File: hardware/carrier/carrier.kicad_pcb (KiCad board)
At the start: 4 copper layers, 165 x 103 mm, 153 parts, among them J1 Harness_4Runner, J2 Pi 4 GPIO, J3 UART, M1 FAN1, M2 FAN2, Q1 BUK7Y4R8-60E, Q2 BUK7Y4R8-60E, Q3 MMBT3904, Q4 MMBT3904, Q5 MMBT3904, Q6 2N7002, Q7 2N7002, U1 LM74800-Q1, U2 ADS1115IDGS, U3 DS3231SN, U4 CAT24C32, U5 LM61460-Q1, U6 TLV75533PDBV, U7 TAS6424E-Q1, U8 CS2100-CP, Y1 12MHz

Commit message: Carrier PCB: Pi geometry from the HAT spec, amplifier block placement
J2 sits on the bottom with pin 1 over the Pi's pin 1 (checked by pad
position), H1-H4 on the Pi hole pattern and isolated per the HAT spec,
USB/Ethernet notch and display-flex cutout follow the Pi's position
(provisional until measured). The TAS6424 block follows TI's EVM layout.
Parts carry a Section field so placement finds them by block and net.
Boot caps move to 0603 to fit the 0.635 mm pitch.

Co-Authored-By: Claude Opus 5.5 <noreply@anthropic.com>
Claude-Session: https://claude.ai/code/session_01EoLoLi7g91W5u4w3UzwQgu
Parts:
- C43, C44, C45, C46, C47, C48, C49, C50: footprint Capacitor_SMD:C_0805_2012Metric -> Capacitor_SMD:C_0603_1608Metric
- H1, H2, H3, H4: footprint MountingHole:MountingHole_2.7mm_M2.5_Pad_Via -> MountingHole:MountingHole_2.7mm_M2.5
- J2: moved to B.Cu
- moved U4 205.7 mm to (118.6, 267.6)
- moved U3 205.7 mm to (106.0, 270.3)
- moved R8 205.1 mm to (113.5, 259.0)
- moved R9 205.1 mm to (119.5, 259.0)
- moved R10 205.1 mm to (125.5, 259.0)
- moved R6 205.1 mm to (101.5, 259.0)
- moved R7 205.1 mm to (107.5, 259.0)
- moved C69 200.6 mm to (322.2, 218.8)
- moved C67 200.6 mm to (310.2, 218.8)
- moved C68 200.6 mm to (316.2, 218.8)
- moved U7 199.8 mm to (208.0, 168.0)
- moved L3 193.9 mm to (240.8, 180.0)
- moved L5 184.2 mm to (240.8, 172.0)
- moved L4 182.9 mm to (226.8, 172.0)
- moved C65 179.5 mm to (246.6, 154.4), turned to 90 degrees
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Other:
- outline, holes or cut-outs redrawn

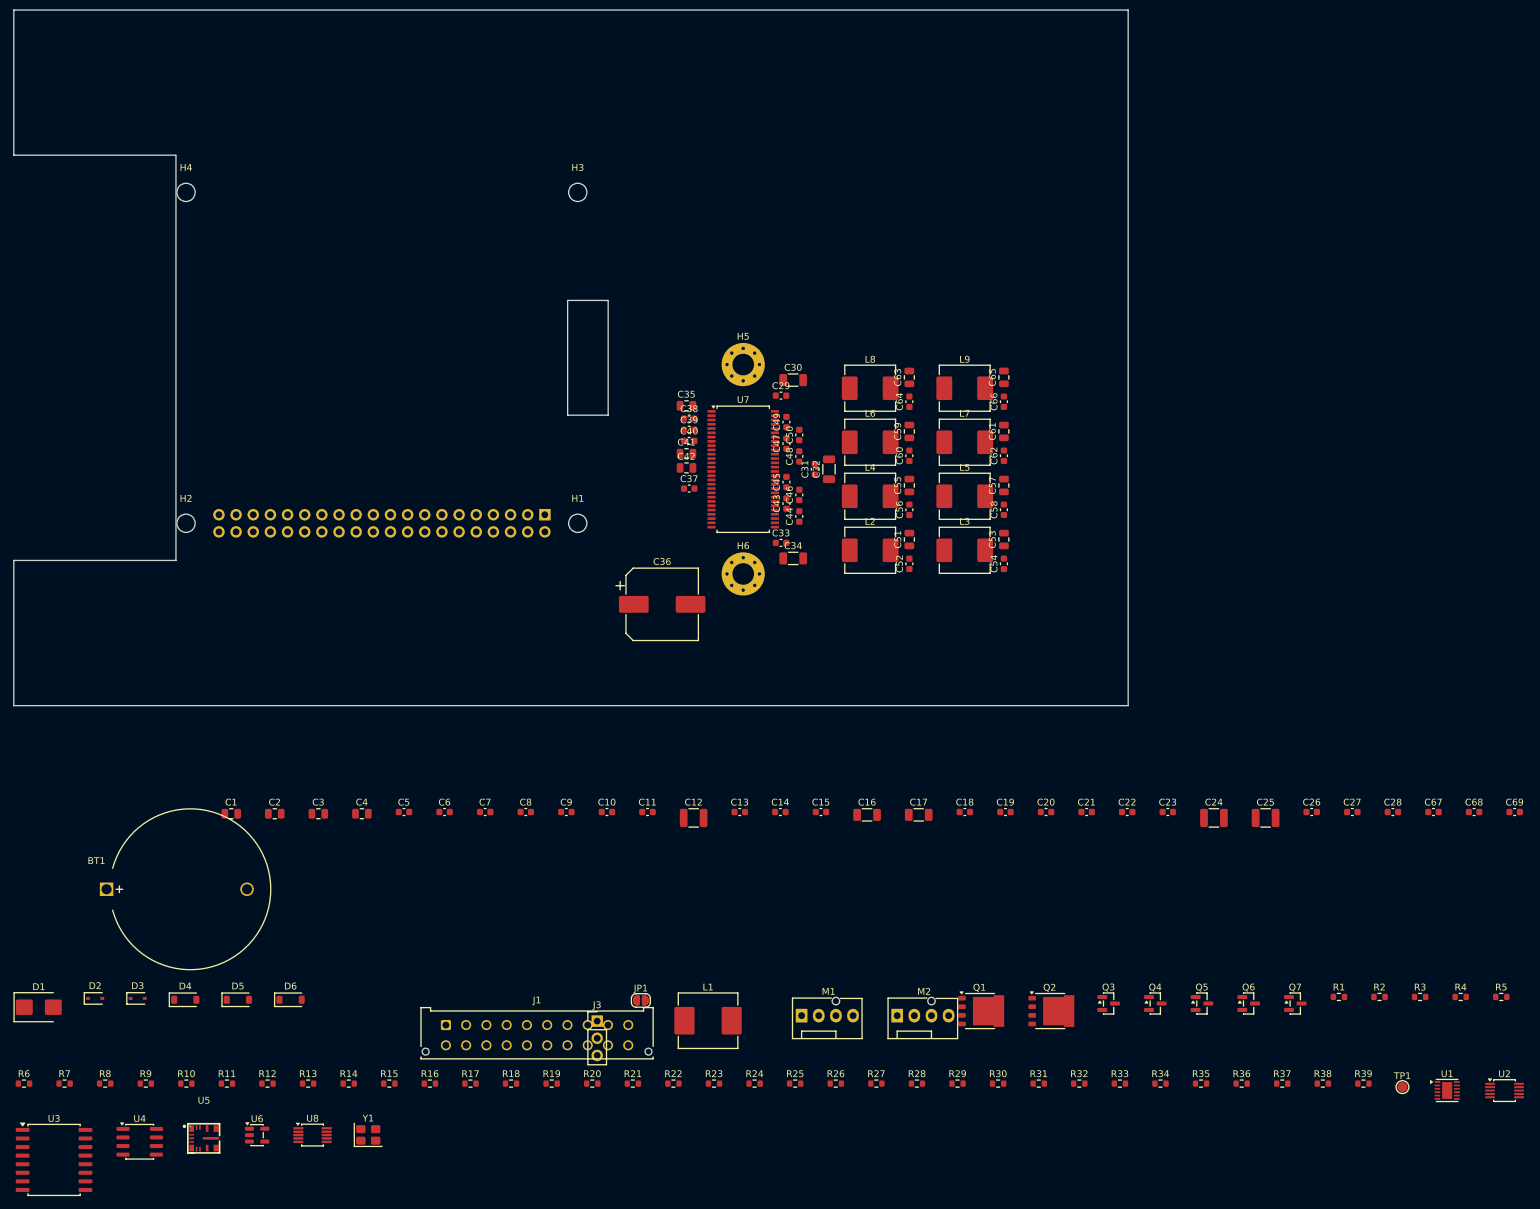
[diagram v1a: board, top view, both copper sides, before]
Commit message: Carrier PCB: place harness, input protection and 5 V buck blocks
Co-Authored-By: Claude Opus 5.5 <noreply@anthropic.com>
Claude-Session: https://claude.ai/code/session_01EoLoLi7g91W5u4w3UzwQgu
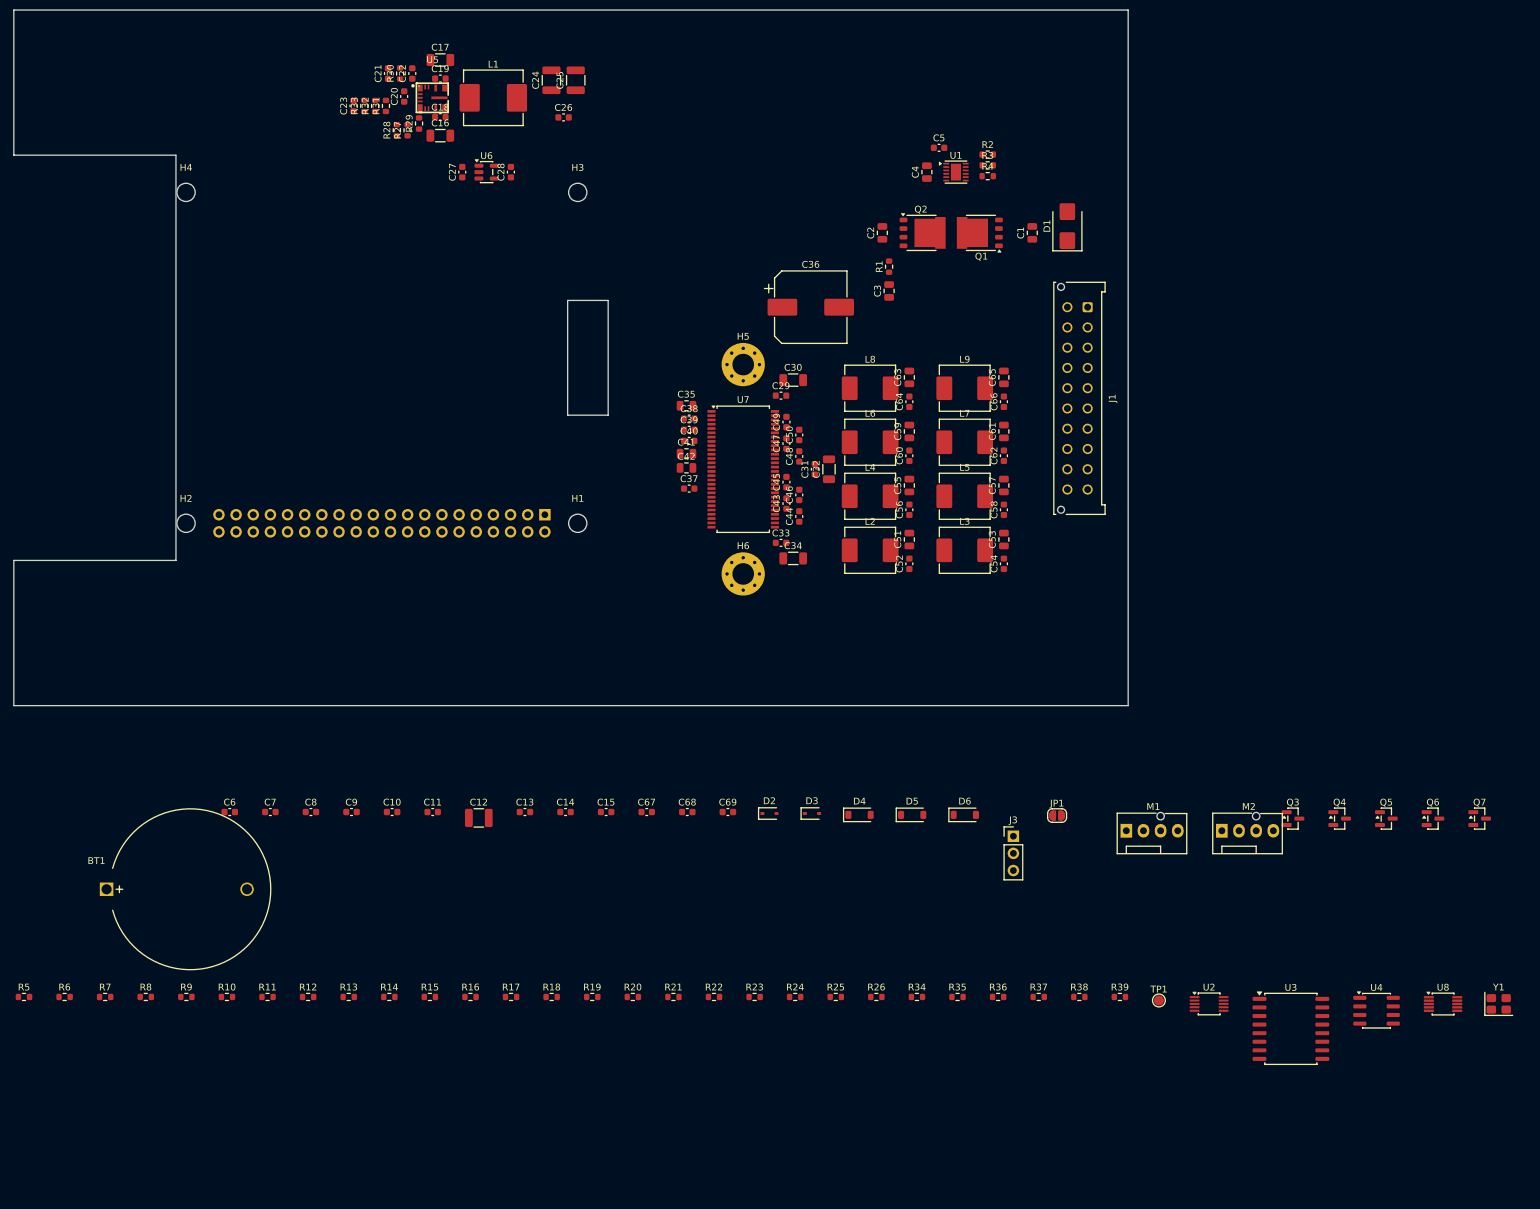
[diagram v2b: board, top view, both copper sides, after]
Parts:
- moved R5 218.7 mm to (101.5, 246.1)
- moved D1 191.2 mm to (256.0, 132.0), turned to 90 degrees
- moved U4 184.2 mm to (301.8, 248.2)
- moved U3 184.2 mm to (289.1, 250.9)
- moved R33 183.0 mm to (151.9, 114.2), turned to 90 degrees
- moved R32 178.4 mm to (153.5, 114.2), turned to 90 degrees
- moved R31 174.1 mm to (155.1, 114.2), turned to 90 degrees
- moved R30 173.8 mm to (157.2, 109.4), turned to 90 degrees
- moved U8 168.5 mm to (311.6, 247.2)
- moved Y1 168.5 mm to (319.9, 247.2)
- moved R29 163.0 mm to (160.0, 116.8), turned to 90 degrees
- moved C27 162.3 mm to (166.4, 124.0), turned to 90 degrees
- moved C28 161.4 mm to (173.6, 124.0), turned to 90 degrees
- moved R28 160.8 mm to (156.7, 117.8), turned to 90 degrees
- moved C23 159.6 mm to (150.3, 114.2), turned to 90 degrees
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
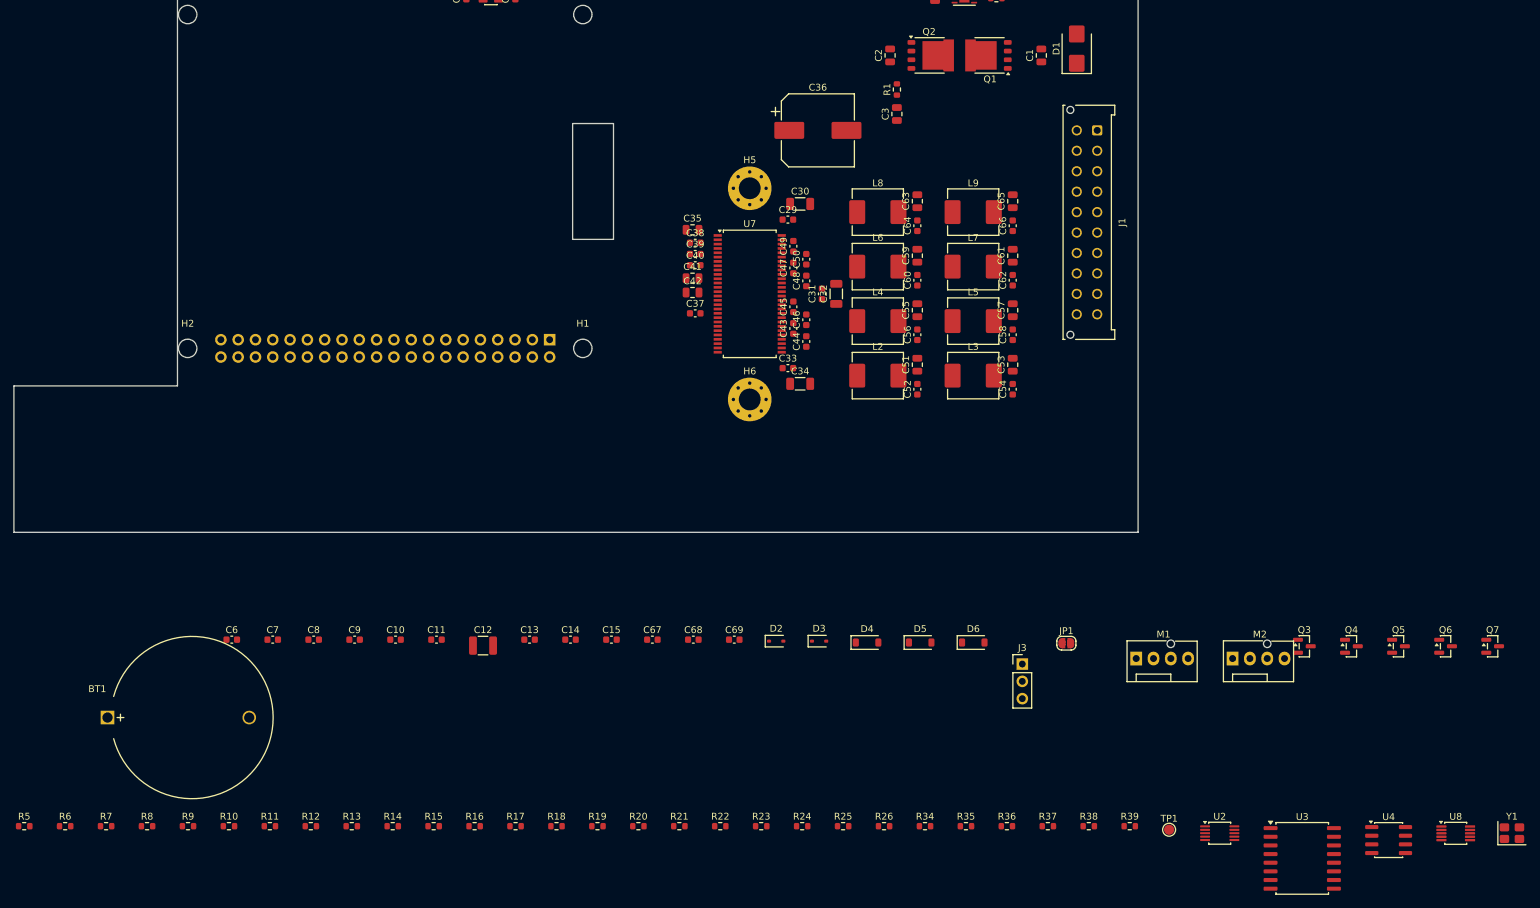
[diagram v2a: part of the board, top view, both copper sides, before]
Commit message: Carrier PCB: place the remaining circuits; every part on the board
RTC, coin cell and ID EEPROM over the Pi, key/lights/reverse sensing and
the wheel ADC beside J1's control pins, fan headers on the bottom edge.
U8 uses the 3x3 TSSOP-10 land pattern (same MO-187 package, wider gaps).
DRC: no overlaps or clearance errors; routing still to do.

Co-Authored-By: Claude Opus 5.5 <noreply@anthropic.com>
Claude-Session: https://claude.ai/code/session_01EoLoLi7g91W5u4w3UzwQgu
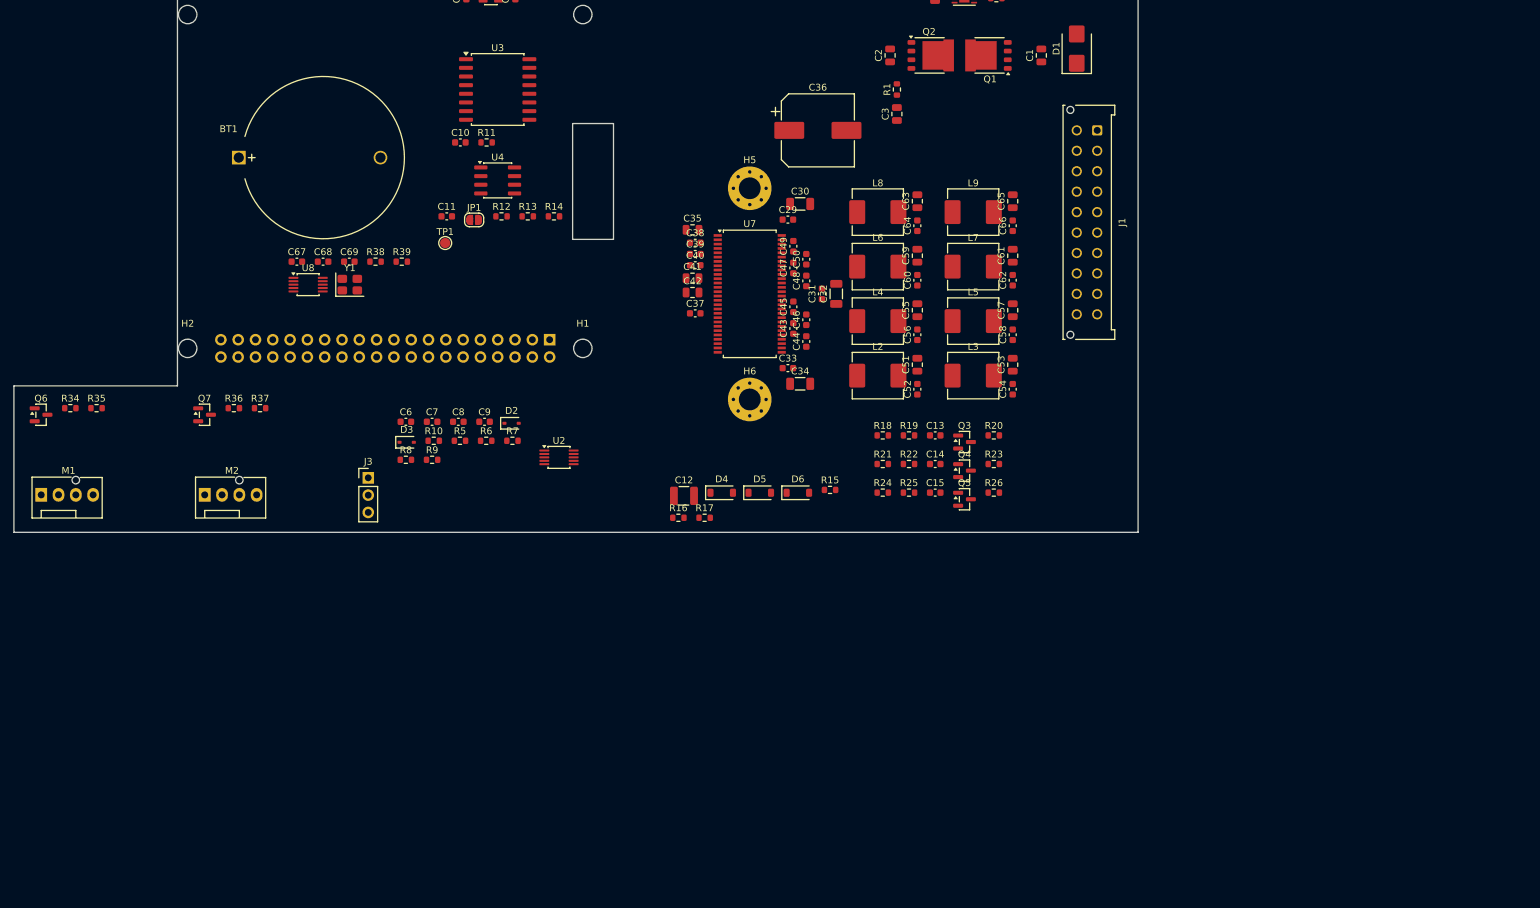
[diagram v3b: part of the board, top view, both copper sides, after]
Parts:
- U8: footprint Package_SO:MSOP-10_3x3mm_P0.5mm -> Package_SO:TSSOP-10_3x3mm_P0.5mm
- moved Q6 208.9 mm to (104.0, 185.7)
- moved Q7 192.1 mm to (128.0, 185.7)
- moved Y1 188.6 mm to (149.3, 166.6)
- moved U8 186.7 mm to (143.2, 166.6)
- moved U3 163.4 mm to (171.0, 138.0)
- moved U4 162.7 mm to (171.0, 151.3)
- moved M1 162.5 mm to (104.0, 197.5)
- moved M2 152.8 mm to (128.0, 197.5)
- moved R35 141.6 mm to (112.1, 184.8)
- moved R34 139.7 mm to (108.3, 184.8)
- moved TP1 136.8 mm to (163.3, 160.5)
- moved R39 135.2 mm to (156.9, 163.3)
- moved R38 133.5 mm to (153.1, 163.3)
- moved R37 130.9 mm to (136.1, 184.8)
- moved R36 129.0 mm to (132.3, 184.8)
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
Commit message: Carrier: board becomes the I2S clock master; amp heatsink design
The Pi's PCM block carries only two channels, so TDM4 cannot feed four
amp channels, and the TAS6424 needs a real MCLK (128-512 fs) outside
TDM. A 12.288 MHz oscillator now drives the amp's MCLK and a PCM1808-Q1
in master mode (MD1 = MD0 = 1) divides it to BCK = 64 fs and LRCK =
48 kHz; the Pi runs its I2S port as a clock consumer. SDIN2 takes the
same data as SDIN1, so the rear speakers play the front stereo pair and
the amp's per-channel volume does the fader. The commercial-grade
CS2100 option is gone.

tools/heatsink.py models a CNC aluminium heatsink after TI's EVM part
(20 x 41.4 mm, four 25 mm fins, feet on the grounded screw pads, M3
tapped from below); its outline is drawn on the board so nothing taller
than 2.2 mm sits under it.

Co-Authored-By: Claude Opus 5.5 <noreply@anthropic.com>
Claude-Session: https://claude.ai/code/session_01EoLoLi7g91W5u4w3UzwQgu
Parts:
- removed Y1: 12MHz, Crystal:Crystal_SMD_3225-4Pin_3.2x2.5mm
- added C70: 10uF, Capacitor_SMD:C_0805_2012Metric, F.Cu at (153.7, 160.6)
- added C71: 100nF, Capacitor_SMD:C_0603_1608Metric, F.Cu at (157.8, 160.4)
- added C72: 10uF, Capacitor_SMD:C_0805_2012Metric, F.Cu at (141.7, 163.5)
- added R40: 33R, Resistor_SMD:R_0603_1608Metric, F.Cu at (153.5, 163.2)
- added X1: 12.288MHz, Oscillator:Oscillator_SMD_Abracon_ASE-4Pin_3.2x2.5mm, F.Cu at (150.7, 167.1)
- C68: value 33pF -> 10uF; footprint Capacitor_SMD:C_0603_1608Metric -> Capacitor_SMD:C_0805_2012Metric
- C69: value 33pF -> 100nF
- R38, R39: value 0R -> 33R
- U8: value CS2100-CP -> PCM1808-Q1; footprint Package_SO:TSSOP-10_3x3mm_P0.5mm -> Package_SO:TSSOP-14_4.4x5mm_P0.65mm
- moved R38 7.26 mm to (145.8, 163.2)
- moved R39 7.26 mm to (149.7, 163.2)
- moved C36 3.64 mm to (217.0, 140.5)
- moved C69 2.93 mm to (149.7, 160.4)
- moved C67 2.90 mm to (141.5, 160.4)
- moved C68 2.66 mm to (145.6, 160.6)
- moved BT1 2.20 mm to (133.0, 145.8)
- moved U8 1.62 mm to (143.9, 168.1)
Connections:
- C68 pad 1: /XTI -> Net-(U8-VREF)
- C69 pad 1: /XTO -> +5V
- R38 pad 1: Net-(U8-CLK_OUT) -> Net-(X1-OUT)
- R39 pad 1: /I2S_BCLK -> Net-(U8-BCK)
- R39 pad 2: /AMP_MCLK -> /I2S_BCLK
- U7 pad 16: GND -> /I2S_DOUT
- U8 pad 1: +3V3 -> Net-(U8-VREF)
- U8 pad 10: /I2C_SDA -> +3V3
- U8 pad 3: Net-(U8-CLK_OUT) -> +5V
- U8 pad 4: unconnected-(U8-AUX_OUT-Pad4) -> +3V3
- U8 pad 5: /I2S_FSYNC -> GND
- U8 pad 6: /XTO -> /AMP_MCLK
- U8 pad 7: /XTI -> Net-(U8-LRCK)
- U8 pad 8: GND -> Net-(U8-BCK)
- U8 pad 9: /I2C_SCL -> unconnected-(U8-DOUT-Pad9)
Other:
- board text added: "HEATSINK 20x41.4 (mech/heatsink.step): parts under it < 2.2 mm"
